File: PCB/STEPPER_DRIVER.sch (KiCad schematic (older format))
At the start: 15 parts, among them J3 STEPPER, J4 STEPPER, U3 DRV8825_BREAKOUT

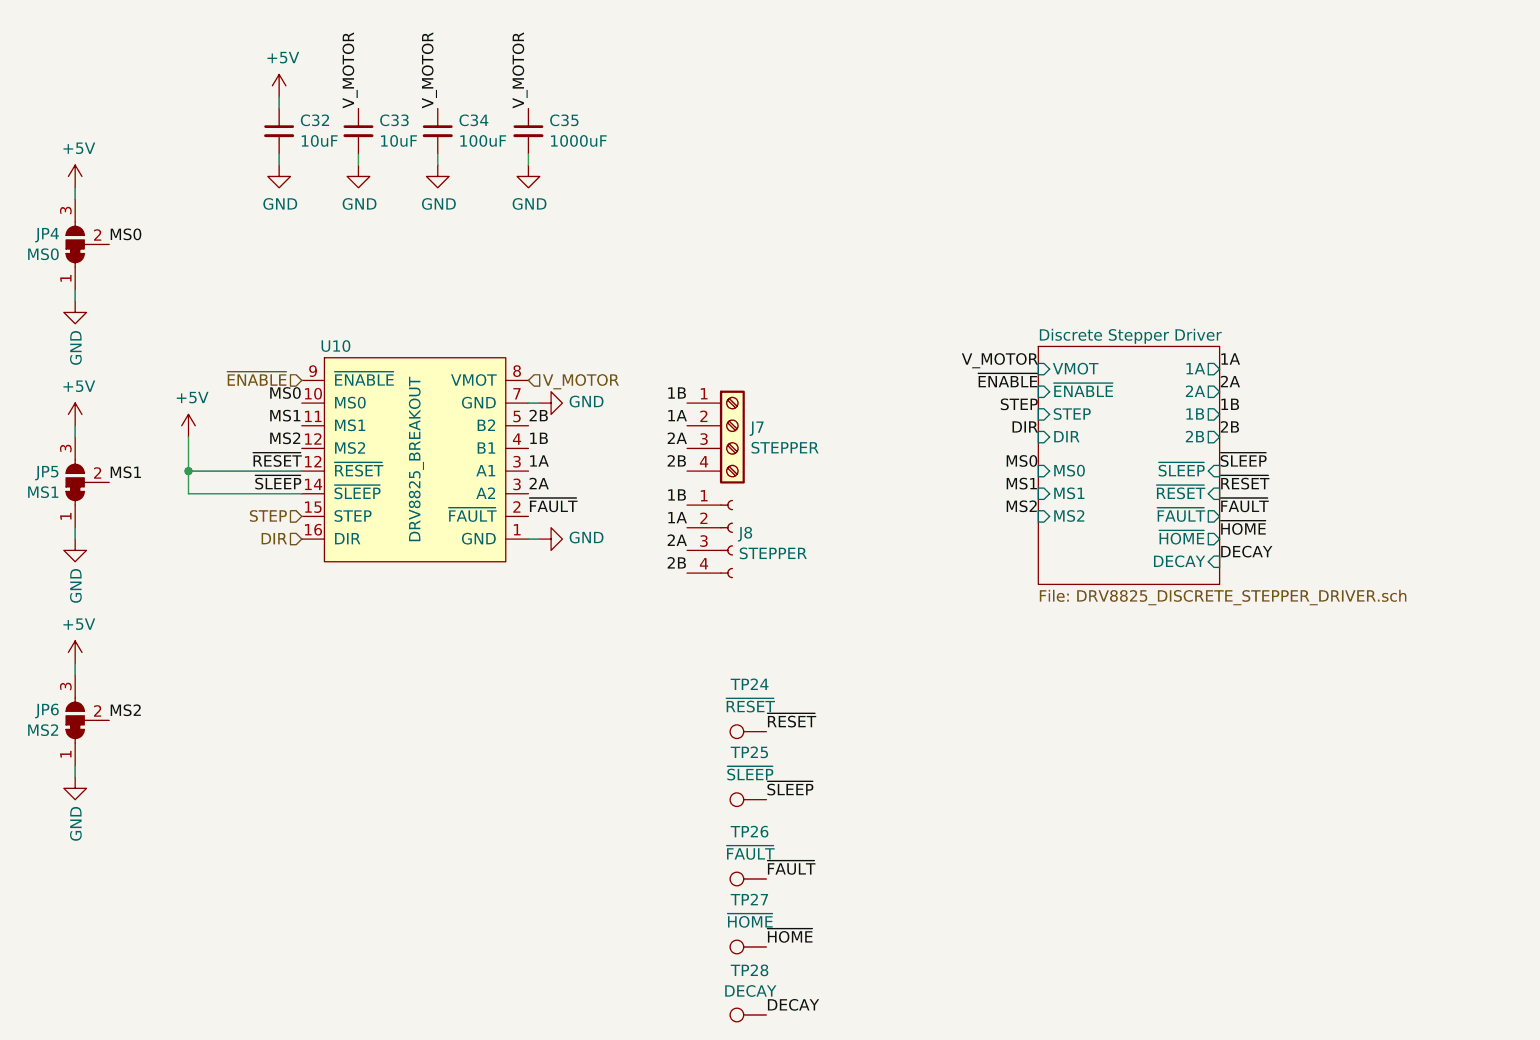
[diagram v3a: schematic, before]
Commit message: Added breakout footprints
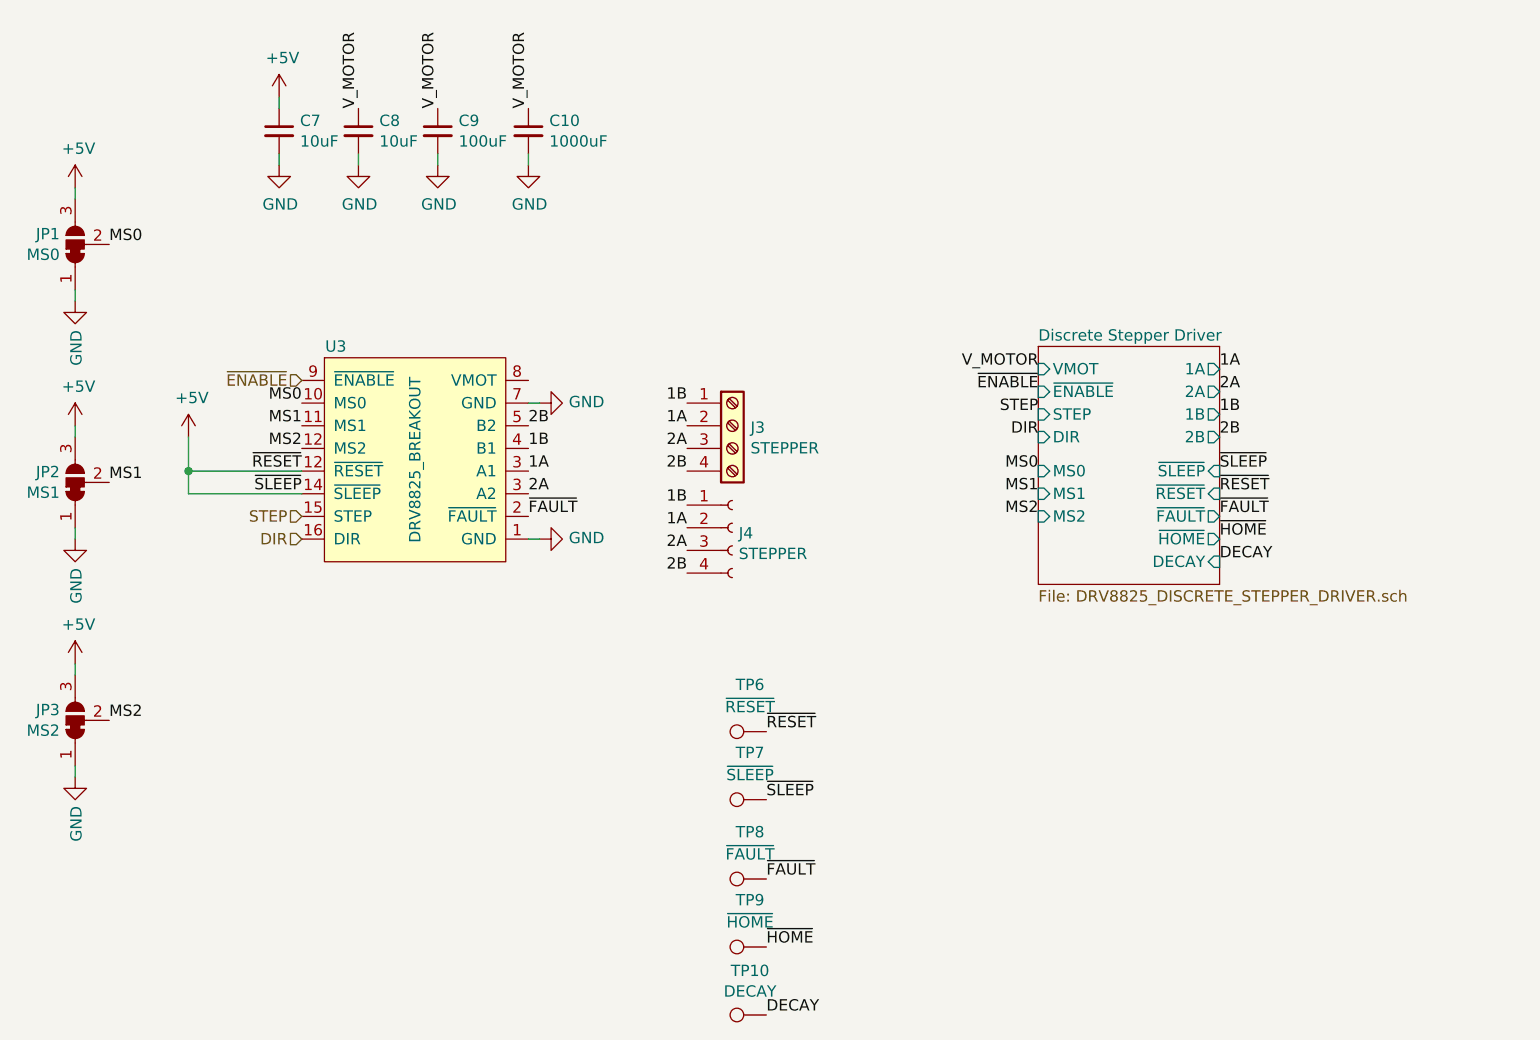
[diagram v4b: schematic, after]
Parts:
- U3: footprint (none) -> Module:Pololu_Breakout-16_15.2x20.3mm
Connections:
- net V_MOTOR: no longer U3.8 (VMOT)
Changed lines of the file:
@@
 AR Path="/5E8A6686/5E8A7820" Ref="J4"  Part="1"
 AR Path="/5E8813FF/5E8A7820" Ref="J8"  Part="1"
-F 0 "J8" H 7278 4226 50  0000 L CNN
+F 0 "J4" H 7278 4226 50  0000 L CNN
 F 1 "STEPPER" H 7278 4135 50  0000 L CNN
 F 2 "" H 7250 4250 50  0001 C CNN
@@
 AR Path="/5E8A6686/5E8A82D9" Ref="J3"  Part="1"
 AR Path="/5E8813FF/5E8A82D9" Ref="J7"  Part="1"
-F 0 "J7" H 7330 3792 50  0000 L CNN
+F 0 "J3" H 7330 3792 50  0000 L CNN
 F 1 "STEPPER" H 7330 3701 50  0000 L CNN
 F 2 "" H 7250 3800 50  0001 C CNN
@@
 AR Path="/5E8A6686/5E842853" Ref="#PWR038"  Part="1"
 AR Path="/5E8813FF/5E842853" Ref="#PWR0103"  Part="1"
-F 0 "#PWR0103" H 6400 4050 50  0001 C CNN
+F 0 "#PWR038" H 6400 4050 50  0001 C CNN
 F 1 "GND" V 6405 4172 50  0000 R CNN
 F 2 "" H 6400 4300 50  0001 C CNN
@@
 AR Path="/5E8A6686/5E842AD6" Ref="#PWR037"  Part="1"
 AR Path="/5E8813FF/5E842AD6" Ref="#PWR0102"  Part="1"
-F 0 "#PWR0102" H 6400 3450 50  0001 C CNN
+F 0 "#PWR037" H 6400 3450 50  0001 C CNN
 F 1 "GND" V 6405 3572 50  0000 R CNN
 F 2 "" H 6400 3700 50  0001 C CNN
@@
 Wire Wire Line
 	6400 4300 6350 4300
-Text HLabel 6350 3600 2    50   Input ~ 0
-V_MOTOR
 Text HLabel 5350 4200 0    50   Input ~ 0
 STEP
@@
 AR Path="/5E8A6686/5E8548E0" Ref="C9"  Part="1"
 AR Path="/5E8813FF/5E8548E0" Ref="C34"  Part="1"
-F 0 "C34" H 6042 2546 50  0000 L CNN
+F 0 "C9" H 6042 2546 50  0000 L CNN
 F 1 "100uF" H 6042 2455 50  0000 L CNN
 F 2 "" H 5950 2500 50  0001 C CNN
@@
 AR Path="/5E8A6686/5E8548E7" Ref="#PWR035"  Part="1"
 AR Path="/5E8813FF/5E8548E7" Ref="#PWR0100"  Part="1"
-F 0 "#PWR0100" H 5950 2400 50  0001 C CNN
+F 0 "#PWR035" H 5950 2400 50  0001 C CNN
 F 1 "GND" H 5955 2477 50  0000 C CNN
 F 2 "" H 5950 2650 50  0001 C CNN
@@
 AR Path="/5E8A6686/5E8572F7" Ref="C8"  Part="1"
 AR Path="/5E8813FF/5E8572F7" Ref="C33"  Part="1"
-F 0 "C33" H 5692 2546 50  0000 L CNN
+F 0 "C8" H 5692 2546 50  0000 L CNN
 F 1 "10uF" H 5692 2455 50  0000 L CNN
 F 2 "" H 5600 2500 50  0001 C CNN
@@
 AR Path="/5E8A6686/5E8572FE" Ref="#PWR034"  Part="1"
 AR Path="/5E8813FF/5E8572FE" Ref="#PWR099"  Part="1"
-F 0 "#PWR099" H 5600 2400 50  0001 C CNN
+F 0 "#PWR034" H 5600 2400 50  0001 C CNN
 F 1 "GND" H 5605 2477 50  0000 C CNN
 F 2 "" H 5600 2650 50  0001 C CNN
@@
 AR Path="/5E8A6686/5E860421" Ref="C7"  Part="1"
 AR Path="/5E8813FF/5E860421" Ref="C32"  Part="1"
-F 0 "C32" H 5342 2546 50  0000 L CNN
+F 0 "C7" H 5342 2546 50  0000 L CNN
 F 1 "10uF" H 5342 2455 50  0000 L CNN
 F 2 "" H 5250 2500 50  0001 C CNN
@@
 AR Path="/5E8A6686/5E860428" Ref="#PWR033"  Part="1"
 AR Path="/5E8813FF/5E860428" Ref="#PWR098"  Part="1"
-F 0 "#PWR098" H 5250 2400 50  0001 C CNN
+F 0 "#PWR033" H 5250 2400 50  0001 C CNN
 F 1 "GND" H 5255 2477 50  0000 C CNN
 F 2 "" H 5250 2650 50  0001 C CNN
@@
 AR Path="/5E8A6686/5E90606A" Ref="#PWR032"  Part="1"
 AR Path="/5E8813FF/5E90606A" Ref="#PWR097"  Part="1"
-F 0 "#PWR097" H 5250 2200 50  0001 C CNN
+F 0 "#PWR032" H 5250 2200 50  0001 C CNN
 F 1 "+5V" H 5265 2523 50  0000 C CNN
 F 2 "" H 5250 2350 50  0001 C CNN
@@
 AR Path="/5E8A6686/5E85775C" Ref="#PWR036"  Part="1"
 AR Path="/5E8813FF/5E85775C" Ref="#PWR0101"  Part="1"
-F 0 "#PWR0101" H 6350 2400 50  0001 C CNN
+F 0 "#PWR036" H 6350 2400 50  0001 C CNN
 F 1 "GND" H 6355 2477 50  0000 C CNN
 F 2 "" H 6350 2650 50  0001 C CNN
@@
 AR Path="/5E8A6686/5E857755" Ref="C10"  Part="1"
 AR Path="/5E8813FF/5E857755" Ref="C35"  Part="1"
-F 0 "C35" H 6442 2546 50  0000 L CNN
+F 0 "C10" H 6442 2546 50  0000 L CNN
 F 1 "1000uF" H 6442 2455 50  0000 L CNN
 F 2 "" H 6350 2500 50  0001 C CNN
@@
 AR Path="/5E8A6686/5E913339" Ref="JP1"  Part="1"
 AR Path="/5E8813FF/5E913339" Ref="JP4"  Part="1"
-F 0 "JP4" V 4396 3068 50  0000 L CNN
+F 0 "JP1" V 4396 3068 50  0000 L CNN
 F 1 "MS0" V 4305 3068 50  0000 L CNN
 F 2 "" H 4350 3000 50  0001 C CNN
@@
 AR Path="/5E8A6686/5E9143CE" Ref="#PWR025"  Part="1"
 AR Path="/5E8813FF/5E9143CE" Ref="#PWR090"  Part="1"
-F 0 "#PWR090" H 4350 2600 50  0001 C CNN
+F 0 "#PWR025" H 4350 2600 50  0001 C CNN
 F 1 "+5V" H 4365 2923 50  0000 C CNN
 F 2 "" H 4350 2750 50  0001 C CNN
@@
 AR Path="/5E8A6686/5E914CAC" Ref="#PWR026"  Part="1"
 AR Path="/5E8813FF/5E914CAC" Ref="#PWR091"  Part="1"
-F 0 "#PWR091" H 4350 3000 50  0001 C CNN
+F 0 "#PWR026" H 4350 3000 50  0001 C CNN
 F 1 "GND" V 4355 3122 50  0000 R CNN
 F 2 "" H 4350 3250 50  0001 C CNN
@@
 AR Path="/5E8A6686/5E916887" Ref="JP2"  Part="1"
 AR Path="/5E8813FF/5E916887" Ref="JP5"  Part="1"
-F 0 "JP5" V 4396 4118 50  0000 L CNN
+F 0 "JP2" V 4396 4118 50  0000 L CNN
 F 1 "MS1" V 4305 4118 50  0000 L CNN
 F 2 "" H 4350 4050 50  0001 C CNN
@@
 AR Path="/5E8A6686/5E91688D" Ref="#PWR027"  Part="1"
 AR Path="/5E8813FF/5E91688D" Ref="#PWR092"  Part="1"
-F 0 "#PWR092" H 4350 3650 50  0001 C CNN
+F 0 "#PWR027" H 4350 3650 50  0001 C CNN
 F 1 "+5V" H 4365 3973 50  0000 C CNN
 F 2 "" H 4350 3800 50  0001 C CNN
@@
 AR Path="/5E8A6686/5E916894" Ref="#PWR028"  Part="1"
 AR Path="/5E8813FF/5E916894" Ref="#PWR093"  Part="1"
-F 0 "#PWR093" H 4350 4050 50  0001 C CNN
+F 0 "#PWR028" H 4350 4050 50  0001 C CNN
 F 1 "GND" V 4355 4172 50  0000 R CNN
 F 2 "" H 4350 4300 50  0001 C CNN
@@
 AR Path="/5E8A6686/5E917232" Ref="JP3"  Part="1"
 AR Path="/5E8813FF/5E917232" Ref="JP6"  Part="1"
-F 0 "JP6" V 4396 5168 50  0000 L CNN
+F 0 "JP3" V 4396 5168 50  0000 L CNN
 F 1 "MS2" V 4305 5168 50  0000 L CNN
 F 2 "" H 4350 5100 50  0001 C CNN
@@
 AR Path="/5E8A6686/5E917238" Ref="#PWR029"  Part="1"
 AR Path="/5E8813FF/5E917238" Ref="#PWR094"  Part="1"
-F 0 "#PWR094" H 4350 4700 50  0001 C CNN
+F 0 "#PWR029" H 4350 4700 50  0001 C CNN
 F 1 "+5V" H 4365 5023 50  0000 C CNN
 F 2 "" H 4350 4850 50  0001 C CNN
@@
 AR Path="/5E8A6686/5E91723F" Ref="#PWR030"  Part="1"
 AR Path="/5E8813FF/5E91723F" Ref="#PWR095"  Part="1"
-F 0 "#PWR095" H 4350 5100 50  0001 C CNN
+F 0 "#PWR030" H 4350 5100 50  0001 C CNN
 F 1 "GND" V 4355 5222 50  0000 R CNN
 F 2 "" H 4350 5350 50  0001 C CNN
@@
 AR Path="/5E8A6686/5E952808" Ref="#PWR031"  Part="1"
 AR Path="/5E8813FF/5E952808" Ref="#PWR096"  Part="1"
-F 0 "#PWR096" H 4850 3700 50  0001 C CNN
+F 0 "#PWR031" H 4850 3700 50  0001 C CNN
 F 1 "+5V" H 4865 4023 50  0000 C CNN
 F 2 "" H 4850 3850 50  0001 C CNN
@@
 AR Path="/5E8A6686/5E972E18" Ref="U3"  Part="1"
 AR Path="/5E8813FF/5E972E18" Ref="U10"  Part="1"
-F 0 "U10" H 5500 4450 50  0000 C CNN
+F 0 "U3" H 5500 4450 50  0000 C CNN
 F 1 "DRV8825_BREAKOUT" V 5850 3950 50  0000 C CNN
-F 2 "" H 6000 3900 50  0001 C CNN
+F 2 "Module:Pololu_Breakout-16_15.2x20.3mm" H 6000 3900 50  0001 C CNN
 F 3 "" H 6000 3900 50  0001 C CNN
 	1    5850 3950
@@
 AR Path="/5E8A6686/5E9970FA" Ref="TP6"  Part="1"
 AR Path="/5E8813FF/5E9970FA" Ref="TP24"  Part="1"
-F 0 "TP24" V 7607 5222 50  0000 C CNN
+F 0 "TP6" V 7607 5222 50  0000 C CNN
 F 1 "~RESET" V 7509 5222 50  0000 C CNN
 F 2 "" H 7600 5150 50  0001 C CNN
@@
 AR Path="/5E8A6686/5E9975F2" Ref="TP7"  Part="1"
 AR Path="/5E8813FF/5E9975F2" Ref="TP25"  Part="1"
-F 0 "TP25" V 7607 5522 50  0000 C CNN
+F 0 "TP7" V 7607 5522 50  0000 C CNN
 F 1 "~SLEEP" V 7509 5522 50  0000 C CNN
 F 2 "" H 7600 5450 50  0001 C CNN
@@
 AR Path="/5E8A6686/5E998E5E" Ref="TP8"  Part="1"
 AR Path="/5E8813FF/5E998E5E" Ref="TP26"  Part="1"
-F 0 "TP26" V 7607 5872 50  0000 C CNN
+F 0 "TP8" V 7607 5872 50  0000 C CNN
 F 1 "~FAULT" V 7509 5872 50  0000 C CNN
 F 2 "" H 7600 5800 50  0001 C CNN
@@
 AR Path="/5E8A6686/5E998E64" Ref="TP9"  Part="1"
 AR Path="/5E8813FF/5E998E64" Ref="TP27"  Part="1"
-F 0 "TP27" V 7607 6172 50  0000 C CNN
+F 0 "TP9" V 7607 6172 50  0000 C CNN
 F 1 "~HOME" V 7509 6172 50  0000 C CNN
 F 2 "" H 7600 6100 50  0001 C CNN
@@
 AR Path="/5E8A6686/5E99966E" Ref="TP10"  Part="1"
 AR Path="/5E8813FF/5E99966E" Ref="TP28"  Part="1"
-F 0 "TP28" V 7595 6472 50  0000 C CNN
+F 0 "TP10" V 7595 6472 50  0000 C CNN
 F 1 "DECAY" V 7504 6472 50  0000 C CNN
 F 2 "" H 7600 6400 50  0001 C CNN

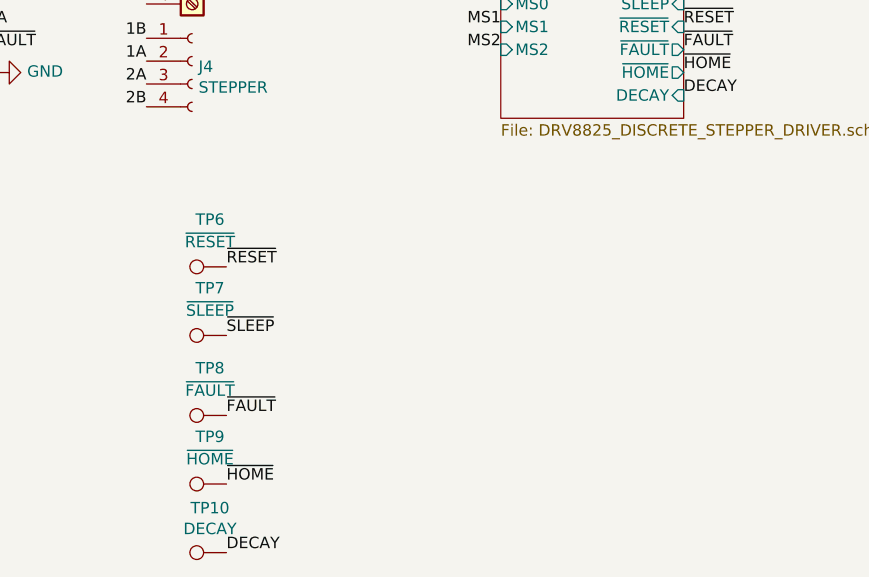
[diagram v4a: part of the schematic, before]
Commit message: Removed unneeded test points
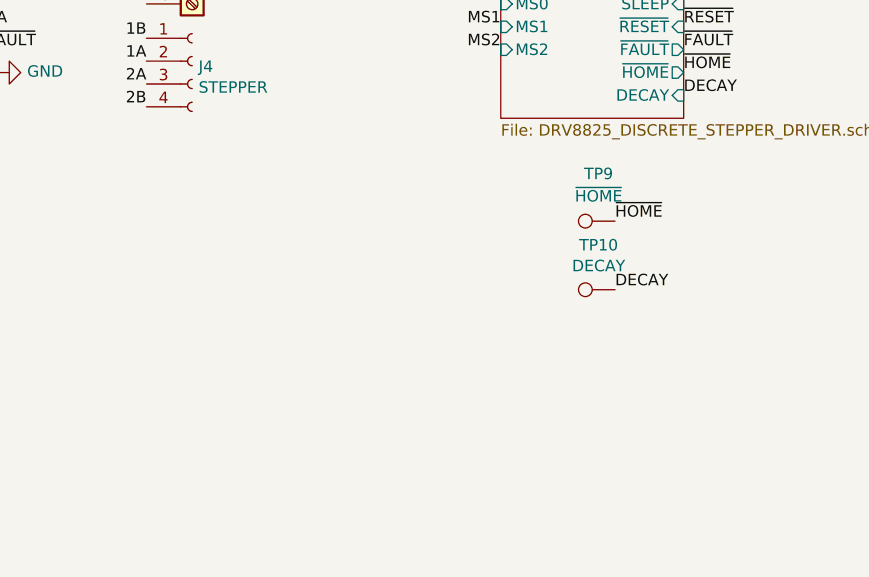
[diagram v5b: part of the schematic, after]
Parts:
- removed TP6: ~RESET, symbol Connector:TestPoint
- removed TP7: ~SLEEP, symbol Connector:TestPoint
- removed TP8: ~FAULT, symbol Connector:TestPoint
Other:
- moved on the sheet: TP10, TP9
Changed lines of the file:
@@
-$Comp
-L Connector:TestPoint TP?
-U 1 1 5E9970FA
-P 7400 5150
-AR Path="/5E9970FA" Ref="TP?"  Part="1"
-AR Path="/5E8A6686/5E9970FA" Ref="TP6"  Part="1"
-AR Path="/5E8813FF/5E9970FA" Ref="TP24"  Part="1"
-F 0 "TP6" V 7607 5222 50  0000 C CNN
-F 1 "~RESET" V 7509 5222 50  0000 C CNN
-F 2 "" H 7600 5150 50  0001 C CNN
-F 3 "~" H 7600 5150 50  0001 C CNN
-	1    7400 5150
-	0    -1   -1   0
-$EndComp
-$Comp
-L Connector:TestPoint TP?
-U 1 1 5E9975F2
-P 7400 5450
-AR Path="/5E9975F2" Ref="TP?"  Part="1"
-AR Path="/5E8A6686/5E9975F2" Ref="TP7"  Part="1"
-AR Path="/5E8813FF/5E9975F2" Ref="TP25"  Part="1"
-F 0 "TP7" V 7607 5522 50  0000 C CNN
-F 1 "~SLEEP" V 7509 5522 50  0000 C CNN
-F 2 "" H 7600 5450 50  0001 C CNN
-F 3 "~" H 7600 5450 50  0001 C CNN
-	1    7400 5450
-	0    -1   -1   0
-$EndComp
-$Comp
-L Connector:TestPoint TP?
-U 1 1 5E998E5E
-P 7400 5800
-AR Path="/5E998E5E" Ref="TP?"  Part="1"
-AR Path="/5E8A6686/5E998E5E" Ref="TP8"  Part="1"
-AR Path="/5E8813FF/5E998E5E" Ref="TP26"  Part="1"
-F 0 "TP8" V 7607 5872 50  0000 C CNN
-F 1 "~FAULT" V 7509 5872 50  0000 C CNN
-F 2 "" H 7600 5800 50  0001 C CNN
-F 3 "~" H 7600 5800 50  0001 C CNN
-	1    7400 5800
-	0    -1   -1   0
-$EndComp
 $Comp
 L Connector:TestPoint TP?
 U 1 1 5E998E64
-P 7400 6100
+P 9100 4950
 AR Path="/5E998E64" Ref="TP?"  Part="1"
 AR Path="/5E8A6686/5E998E64" Ref="TP9"  Part="1"
 AR Path="/5E8813FF/5E998E64" Ref="TP27"  Part="1"
-F 0 "TP9" V 7607 6172 50  0000 C CNN
-F 1 "~HOME" V 7509 6172 50  0000 C CNN
-F 2 "" H 7600 6100 50  0001 C CNN
-F 3 "~" H 7600 6100 50  0001 C CNN
-	1    7400 6100
+F 0 "TP9" V 9307 5022 50  0000 C CNN
+F 1 "~HOME" V 9209 5022 50  0000 C CNN
+F 2 "" H 9300 4950 50  0001 C CNN
+F 3 "~" H 9300 4950 50  0001 C CNN
+	1    9100 4950
 	0    -1   -1   0
 $EndComp
@@
 L Connector:TestPoint TP?
 U 1 1 5E99966E
-P 7400 6400
+P 9100 5250
 AR Path="/5E99966E" Ref="TP?"  Part="1"
 AR Path="/5E8A6686/5E99966E" Ref="TP10"  Part="1"
 AR Path="/5E8813FF/5E99966E" Ref="TP28"  Part="1"
-F 0 "TP10" V 7595 6472 50  0000 C CNN
-F 1 "DECAY" V 7504 6472 50  0000 C CNN
-F 2 "" H 7600 6400 50  0001 C CNN
-F 3 "~" H 7600 6400 50  0001 C CNN
-	1    7400 6400
+F 0 "TP10" V 9295 5322 50  0000 C CNN
+F 1 "DECAY" V 9204 5322 50  0000 C CNN
+F 2 "" H 9300 5250 50  0001 C CNN
+F 3 "~" H 9300 5250 50  0001 C CNN
+	1    9100 5250
 	0    -1   -1   0
 $EndComp
 Text Label 9400 4200 0    50   ~ 0
 ~FAULT
-Text Label 7400 5800 0    50   ~ 0
-~FAULT
-Text Label 7400 5450 0    50   ~ 0
-~SLEEP
-Text Label 7400 5150 0    50   ~ 0
-~RESET
 Text Label 9400 4300 0    50   ~ 0
 ~HOME
 Text Label 9400 4400 0    50   ~ 0
 DECAY
-Text Label 7400 6400 0    50   ~ 0
+Text Label 9100 5250 0    50   ~ 0
 DECAY
-Text Label 7400 6100 0    50   ~ 0
+Text Label 9100 4950 0    50   ~ 0
 ~HOME
 Text Label 6350 4200 0    50   ~ 0
